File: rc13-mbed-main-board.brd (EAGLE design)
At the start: 100 x 80 mm, 54 parts, among them IC1 MBED_MICROCONTROLLER, U1 PCA9555PW,118, X1 BALL_SENS, X2 ETH, X5 BTNS, X9 COIL

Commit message: Routed some board
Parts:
- removed LED3, LED4, LED5: (no value), led:CHIP-LED0603
- removed R31, R32, R33, R34, R8: 2K2, rcl:R0603
- moved LED2 82.1 mm to (17.4, 11.3), turned to 180 degrees
- moved LED1 79.6 mm to (19.5, 11.2), turned to 0 degrees
- moved LED_5V 78.8 mm to (70.7, 3.70), flipped to the top, turned to 90 degrees
- moved R7 77.7 mm to (17.4, 14.4), turned to 90 degrees
- moved R15 75.2 mm to (67.4, 3.70), flipped to the top, turned to 180 degrees
- moved R6 75.0 mm to (19.5, 14.4), turned to 90 degrees
- moved C14 63.9 mm to (41.7, 28.0)
- moved R30 62.0 mm to (41.6, 40.7), turned to 0 degrees
- moved R28 59.7 mm to (41.6, 43.3), turned to 0 degrees
- moved C18 59.3 mm to (41.7, 30.5), turned to 180 degrees
- moved R25 57.7 mm to (41.6, 45.7), turned to 0 degrees
- moved R22 55.9 mm to (41.6, 48.3), turned to 0 degrees
- moved R19 54.4 mm to (41.6, 50.8), turned to 0 degrees
- moved BAT_15V 53.8 mm to (96.0, 66.0)
- moved R13 53.6 mm to (90.9, 68.6), flipped to the top
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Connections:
- removed net LED2: R7.2
- removed net LED3: R8.2
- removed net LED4: R33.2
- removed net LED5: R34.2, U1.20
- removed net N$10: LED_5V.A, R15.2
- removed net N$11: LED4.A, R33.1
- removed net N$12: LED5.A, R34.1
- removed net N$15: R15.1
- removed net SCL2: IC1.27, R32.1
- removed net SDA2: IC1.28, R31.1
- net +3V3: now also LED1.A; no longer R31.2, R32.2
- net +5V: now also R15.2
- net BALL: now also IC1.28
- net CHARGE: now also IC1.20; no longer IC1.19
- net GND: now also LED_5V.A; no longer LED1.C, LED3.C, LED4.C, LED5.C
- net KICK: now also IC1.19; no longer IC1.20
- net LED1: now also R7.2, U1.20
- net N$7: now also LED1.C; no longer LED1.A
- net N$9: now also LED_5V.C, R15.1; no longer LED3.A, R8.1
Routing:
- net +5V: track 0.00 -> 209.8 mm, vias 0 -> 1
- net +3V3: track 1.67 -> 71.2 mm, vias 0 -> 1
- net PWM3: track 0.57 -> 45.2 mm, vias 0 -> 1
- net LED1: track 0.00 -> 40.2 mm
- net PWM4: track 0.00 -> 39.2 mm
- net BTN2: track 0.00 -> 38.4 mm
- net BTN1: track 0.00 -> 32.2 mm
- net SCL: track 0.18 -> 29.6 mm, vias 0 -> 1
- net SDA: track 0.00 -> 28.7 mm, vias 0 -> 1
- net TD+: track 0.00 -> 22.0 mm
- net INT: track 0.06 -> 21.0 mm, vias 0 -> 1
- net TD-: track 0.00 -> 16.2 mm
- net RD+: track 0.00 -> 15.7 mm
- net CHARGE: track 0.00 -> 12.3 mm
- net TACHO2: track 38.8 -> 50.4 mm
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- added copper zone on layer 1, net +15V
- added copper zone on layer 1, net GND
- added copper zone on layer 16, net GND

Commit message: Routed some board
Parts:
- moved LED_5V 1.10 mm to (70.6, 4.80)
- moved R15 1.10 mm to (67.3, 4.80)
- moved R3 0.30 mm to (8.80, 29.6), flipped to the top, turned to 0 degrees
- moved R4 0.30 mm to (21.1, 29.6), flipped to the top, turned to 180 degrees
- moved X5 0.14 mm to (25.1, 9.90), turned to 180 degrees
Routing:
- net +5V: track 209.8 -> 225.0 mm, vias 1 -> 2
- net BTN2: track 38.4 -> 32.2 mm
- net COAST4: track 32.9 -> 36.1 mm
- net BRAKE4: track 30.6 -> 32.5 mm
- net BTN1: track 32.2 -> 33.3 mm
- net RD-: track 9.99 -> 9.31 mm
- net PWM5: track 63.8 -> 64.5 mm
- net DIR4: track 28.3 -> 28.8 mm
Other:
- board size 100 x 80 mm -> 100 x 76 mm

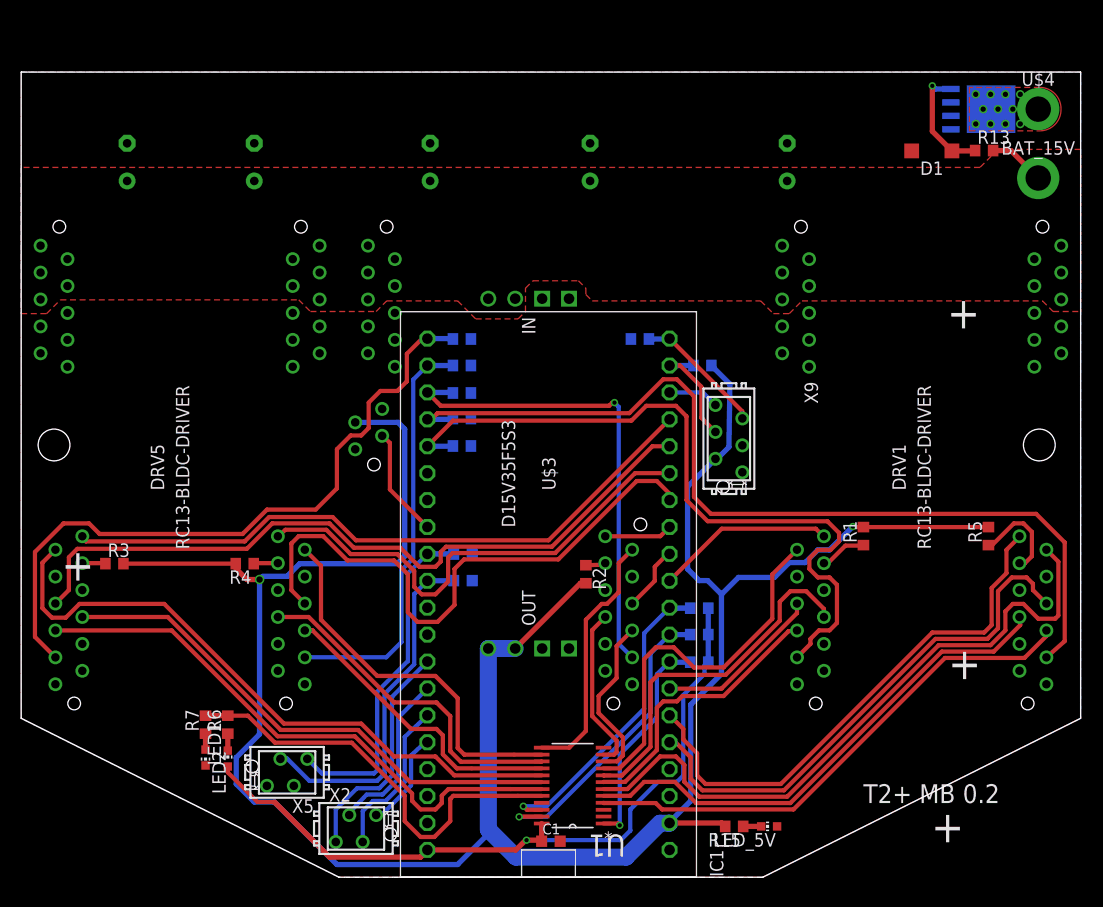
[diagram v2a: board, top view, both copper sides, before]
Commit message: Moved bottom drivers together to make room on the sides
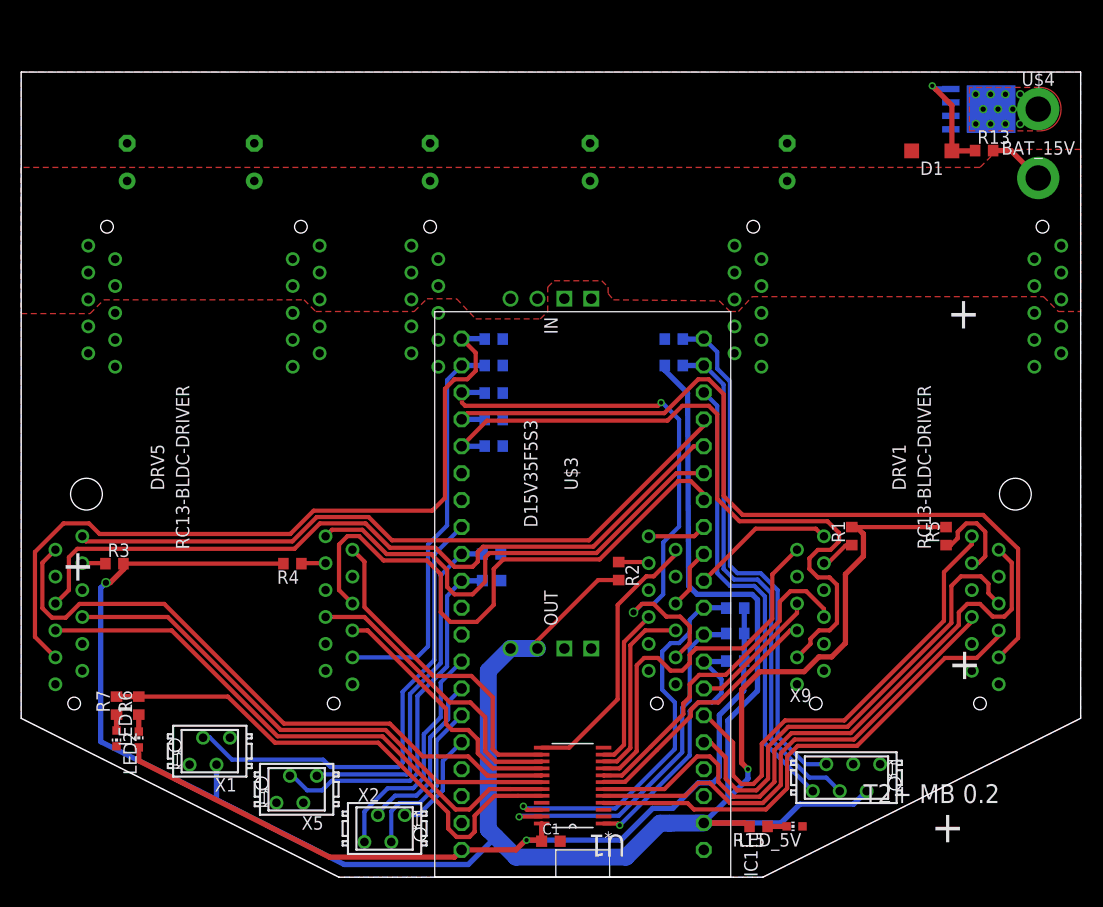
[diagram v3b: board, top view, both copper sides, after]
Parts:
- moved X1 33.9 mm to (17.8, 11.9), flipped to the top, turned to 180 degrees
- moved X9 33.9 mm to (77.9, 9.40), turned to 0 degrees
- moved LED1 8.59 mm to (11.1, 13.0)
- moved R6 8.59 mm to (11.1, 16.2)
- moved LED2 8.59 mm to (9.00, 13.1)
- moved R7 8.59 mm to (9.00, 16.2)
- moved DRV2 4.50 mm to (65.5, 15.0)
- moved DRV4 4.50 mm to (4.50, 15.0)
- moved R4 4.50 mm to (25.6, 29.6)
- moved DRV3 4.10 mm to (35.0, 15.0)
- moved R5 4.00 mm to (87.3, 32.2)
- moved R11 3.40 mm to (67.4, 20.4)
- moved R14 3.40 mm to (67.4, 23.0)
- moved R9 3.40 mm to (67.4, 25.4)
- moved IC1 3.23 mm to (53.0, 25.4)
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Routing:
- net KICK: track 10.9 -> 49.7 mm
- net DONE: track 4.82 -> 43.2 mm
- net CHARGE: track 12.3 -> 49.4 mm
- net BALL: track 10.4 -> 44.7 mm
- net +5V: track 225.0 -> 252.1 mm
- net +3V3: track 71.2 -> 81.4 mm
- net PWM3: track 45.5 -> 55.2 mm, vias 1 -> 2
- net LED1: track 40.7 -> 49.0 mm
- net PWM2: track 87.7 -> 79.6 mm
- net PWM5: track 64.5 -> 72.1 mm
- net SCL: track 29.6 -> 36.8 mm
- net DIRO2: track 50.6 -> 44.4 mm
- net TACHO2: track 50.4 -> 44.7 mm
- net SDA: track 28.7 -> 34.2 mm
- net COAST4: track 36.1 -> 31.3 mm
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
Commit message: Added mounting slots on the sides
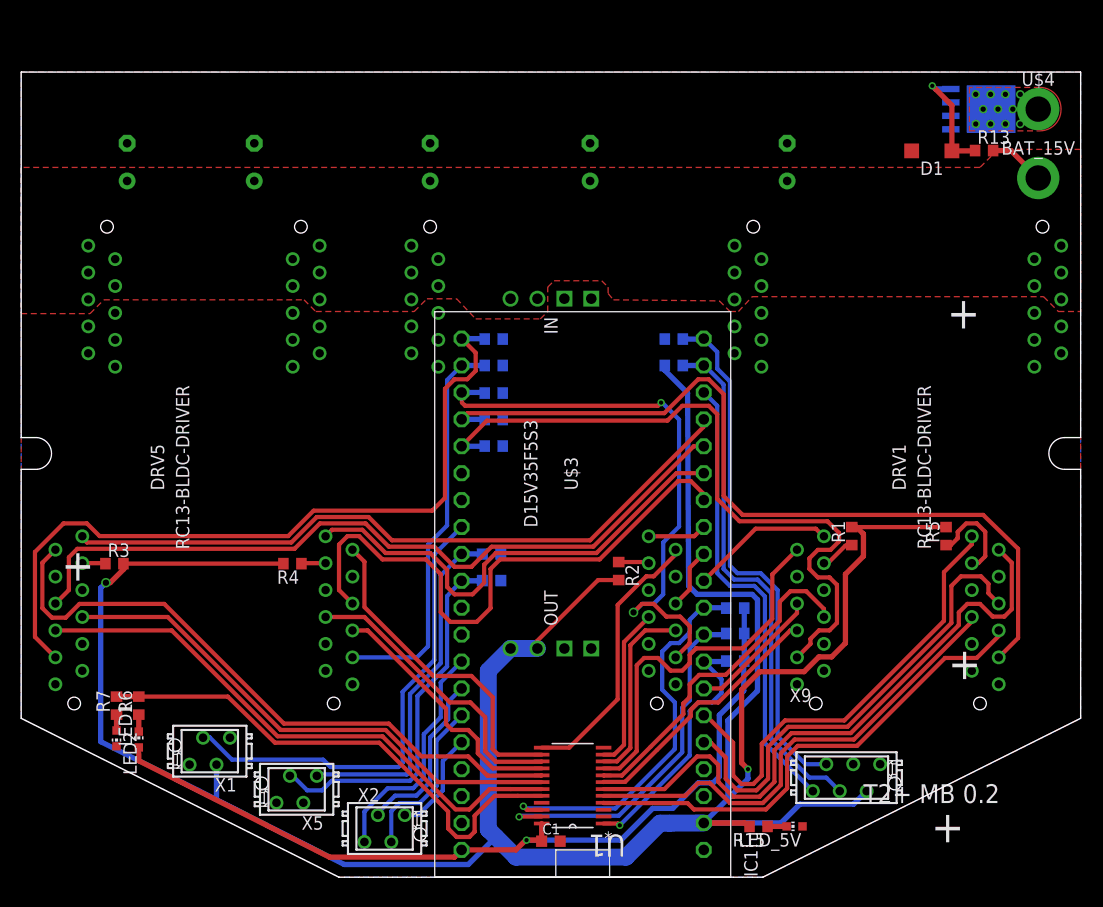
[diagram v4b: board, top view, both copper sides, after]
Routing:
- net TACHO5: track 73.1 -> 72.6 mm
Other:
- outline, holes or cut-outs redrawn

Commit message: Some routing changes
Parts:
- removed C3, C4: 470uF, rcl:E3,5-8
- moved C2 11.4 mm to (50.0, 67.5)
- moved C7 3.00 mm to (25.0, 67.5)
- moved C9 2.70 mm to (75.0, 67.5)
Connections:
- net +15V: no longer C3.+, C4.+
- net GND: no longer C3.-, C4.-
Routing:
- net KICK: track 49.7 -> 51.2 mm
- net DONE: track 43.2 -> 44.7 mm
- net COAST3: track 25.9 -> 24.6 mm
- net CHARGE: track 49.4 -> 50.5 mm
- net TACHO4: track 55.1 -> 55.9 mm
- net TACHO5: track 72.6 -> 73.4 mm
- net PWM5: track 72.2 -> 71.5 mm
- net SCL: track 36.8 -> 37.4 mm
- net RD-: track 9.83 -> 9.22 mm
- net DIRO4: track 45.2 -> 45.8 mm
- net SDA: track 34.2 -> 33.7 mm
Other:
- board text added: "BALL"
- board text added: "BTNS"
- board text added: "COIL"
- board text added: "ETH"
- board text removed: "M1"
- board text removed: "M2"
- board text removed: "M3"

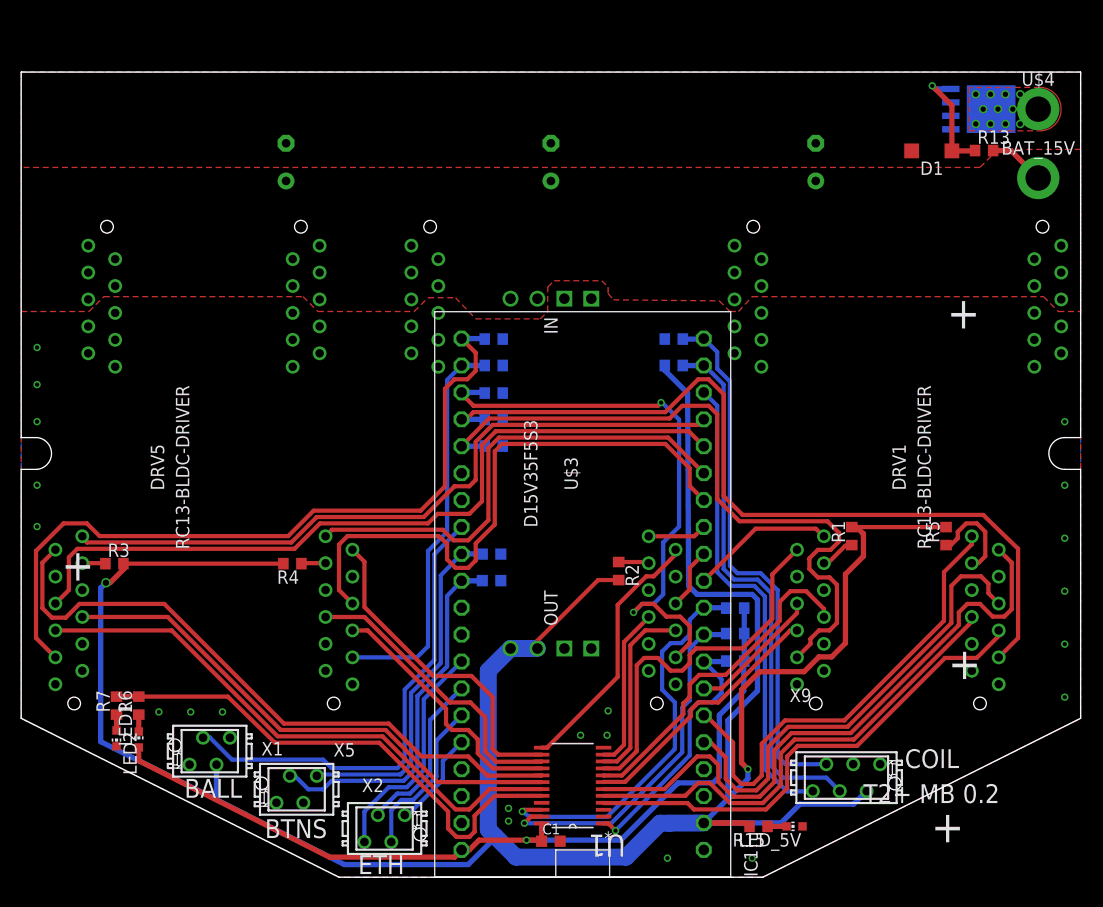
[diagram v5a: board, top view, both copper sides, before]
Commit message: Fixed micromatch pin layout
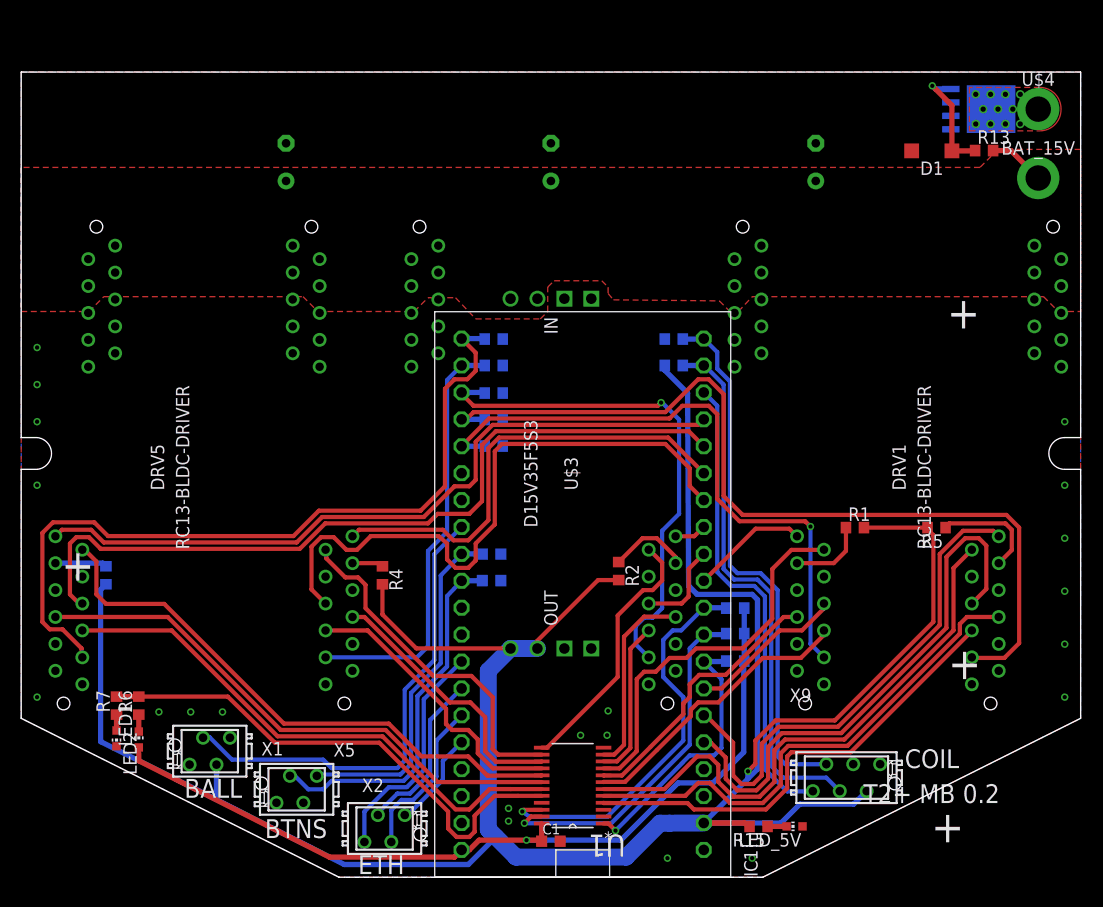
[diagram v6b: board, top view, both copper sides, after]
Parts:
- moved R4 8.57 mm to (34.1, 28.5), turned to 270 degrees
- moved R3 1.36 mm to (8.00, 28.5), flipped to the bottom, turned to 270 degrees
- moved R5 1.20 mm to (86.4, 33.0), turned to 180 degrees
- moved R1 0.85 mm to (78.7, 33.0), turned to 0 degrees
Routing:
- net PWM1: track 66.7 -> 59.1 mm, vias 0 -> 1
- net TACHO2: track 44.7 -> 51.6 mm
- net COAST5: track 60.8 -> 54.0 mm
- net BRAKE1: track 31.8 -> 25.8 mm
- net COAST2: track 59.2 -> 53.4 mm
- net +5V: track 252.1 -> 246.4 mm, vias 2 -> 1
- net PWM3: track 54.7 -> 49.2 mm, vias 2 -> 1
- net N$6: track 2.87 -> 7.62 mm
- net PWM2: track 79.5 -> 83.8 mm
- net N$2: track 3.32 -> 7.30 mm
- net DIRO2: track 44.4 -> 48.1 mm
- net TACHO4: track 55.9 -> 59.4 mm
- net DIRO5: track 65.9 -> 68.9 mm
- net TACHO3: track 5.79 -> 8.66 mm
- net BRAKE3: track 15.3 -> 18.2 mm
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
